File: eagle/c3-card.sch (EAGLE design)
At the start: 111 parts, among them J1 J-SAMTEC-TFM-110-X1-XXX-D-RA, J2 U.FL, J3 U.FL, J4 U.FL, J6 J-SAMTEC-TFM-120-X1-XXX-D-RA, J7 FTSH-105-XX-X-DV-K, Q3 MOSFET-PCH-SOT23-6, Q4 MOSFET-PCH-SOT23-6, Q5 PMV45EN, Q6 PMV45EN, U1 TCAN330, U2 IS21ES04G-JCLI-TR, U3 MAX7310ATE, U4 MAX4211CETE, U5 TPS62111RSA, U6 TCAN330, U7 MCP1703A, X1 16MHZ-2.5x2mm

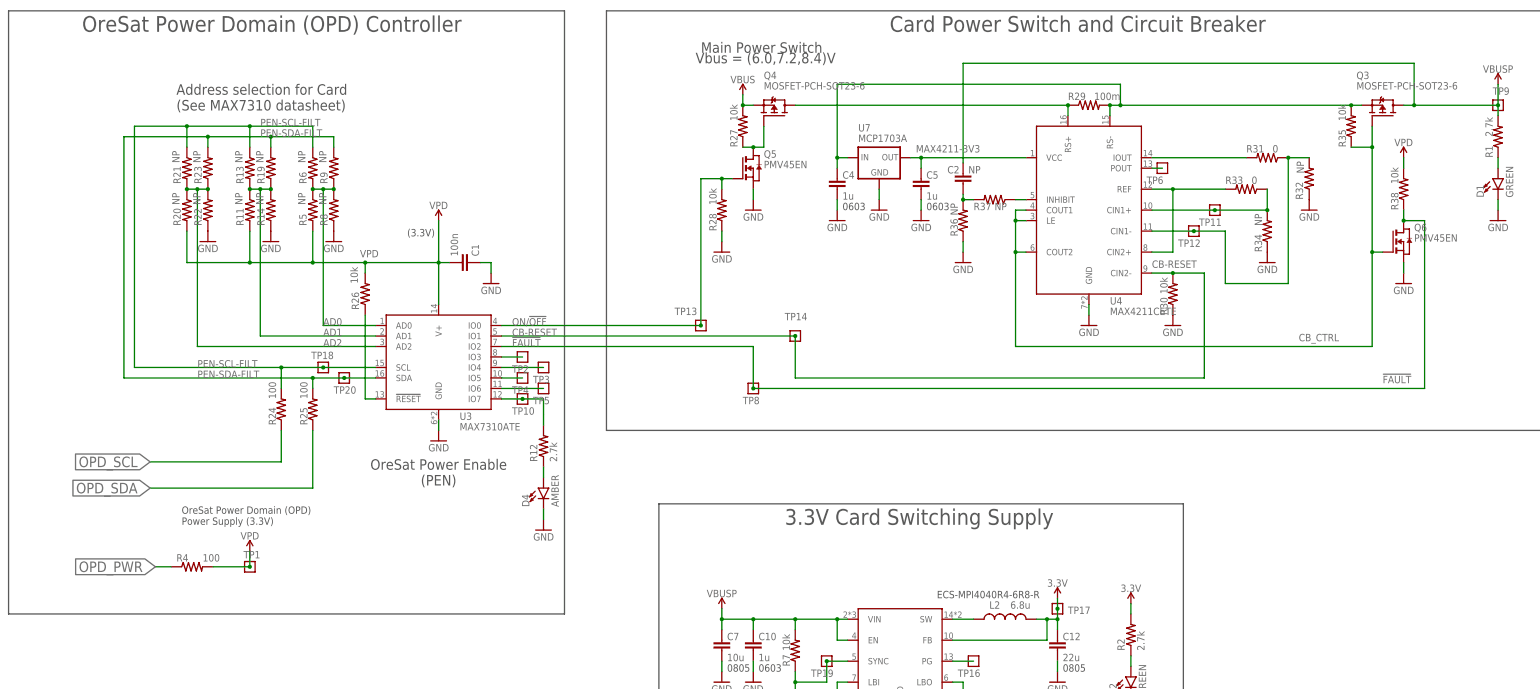
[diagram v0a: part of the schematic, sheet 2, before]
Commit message: Updated to the latest card outline. Updated OreSat main connector pinout. Got rid of some junk we don't need for C3.
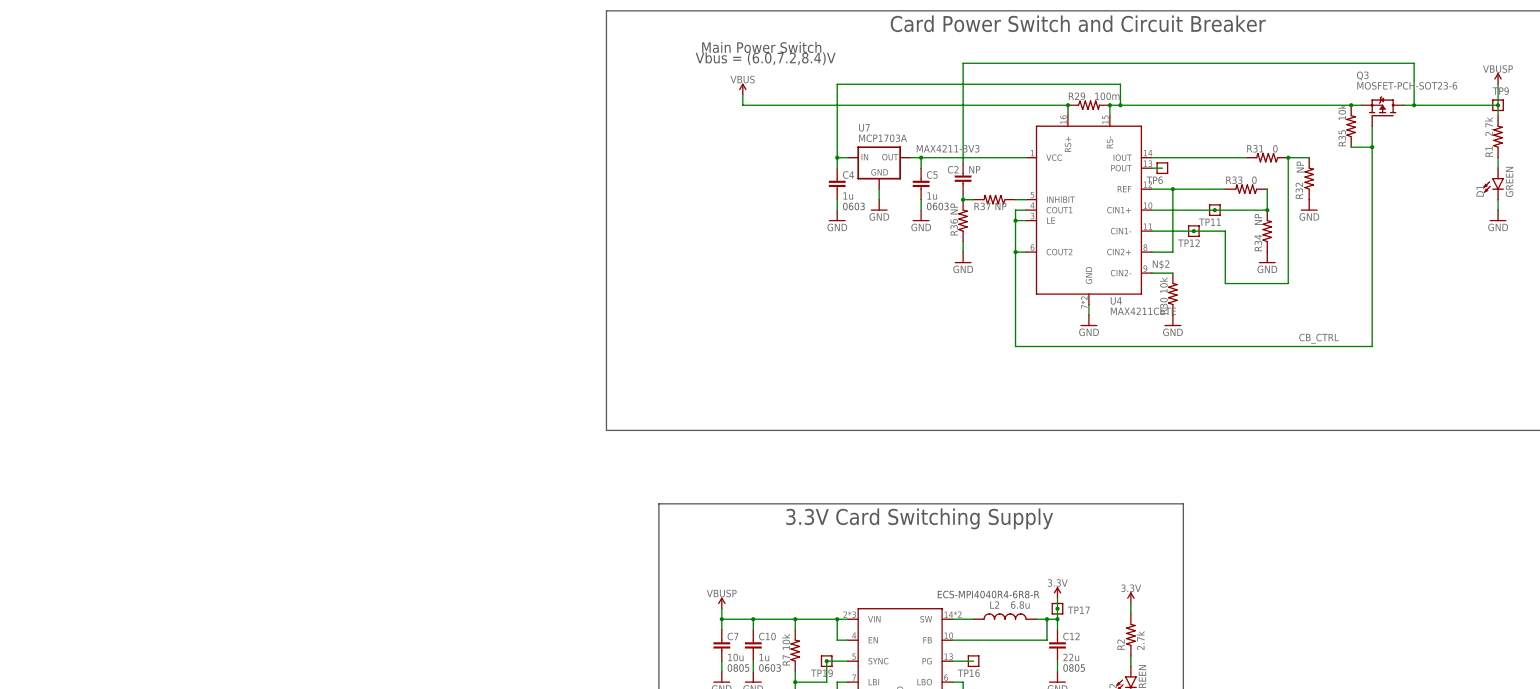
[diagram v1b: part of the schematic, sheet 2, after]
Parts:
- removed C1: 100n, rcl_custom:C-EU0402-B-NOSILK
- removed D4: AMBER, SparkFun-LED:LED-GREEN0603
- removed J1: J-SAMTEC-TFM-110-X1-XXX-D-RA, J-Samtec-TFM-110-X1-XXX-D-RA:J-SAMTEC-TFM-110-X1-XXX-D-RA
- removed J5: (no value), SparkFun-Connectors:6_PIN_SERIAL_TARGETSILK
- removed JP8: (no value), pinhead:PINHD-1X2
- removed Q4: MOSFET-PCH-SOT23-6, Q-MOSFET-PCH-SOT23-6:MOSFET-PCH-SOT23-6
- removed Q5, Q6: PMV45EN, Tova:PMV45EN
- removed R11, R13, R14, R19, R20, R21, R22, R23, R5, R6, R8, R9: NP, rcl_custom:R-US_0402-B-NOSILK
- removed R12: 2.7k, rcl_custom:R-US_0402-B-NOSILK
- removed R24, R25, R4: 100, rcl_custom:R-US_0402-B-NOSILK
- removed R26, R27, R28, R38: 10k, rcl_custom:R-US_0402-B-NOSILK
- removed TP1, TP10, TP13, TP14, TP18, TP2, TP20, TP3, TP4, TP5, TP8: TEST-POINT, Tova:TEST-POINT
- removed U3: MAX7310ATE, U-Maxim-MAX7310-I2C-GPIO-expander:MAX7310
- U$2: value ORESAT-CARD-V1.1 -> ORESAT-CARD-V1.1-3XRF; device oresat-cards:ORESAT-CARD-V1.1 -> oresat-cards:ORESAT-CARD-V1.1-3XRF
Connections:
- net !SHUTDOWN renamed !SD
- removed net !FAULT: Q6.D, R38.1, TP8.1, U3.IO2
- removed net AD0: R5.1, R6.2, R8.2, R9.1, U3.AD0
- removed net AD1: R11.1, R13.2, R14.2, R19.1, U3.AD1
- removed net AD2: R20.1, R21.2, R22.2, R23.1, U3.AD2
- removed net AUX_!SHUTDOWN: J1.19, J1.20
- removed net AUX_CAN1_H: J1.13, J1.14
- removed net AUX_CAN1_L: J1.15, J1.16
- removed net AUX_CAN2_H: J1.1, J1.2
- removed net AUX_CAN2_L: J1.3, J1.4
- removed net AUX_GND1: J1.17, J1.18
- removed net AUX_GND2: J1.11, J1.12
- removed net AUX_GND3: J1.10, J1.9
- removed net AUX_VBUS1: J1.7, J1.8
- removed net AUX_VBUS2: J1.5, J1.6
- removed net CB-RESET: R30.2, TP14.1, U3.IO1, U4.CIN2-
- removed net N$406: J5.VCC, JP8.2
- removed net N$480: TP2.1, U3.IO3
- removed net N$482: TP3.1, U3.IO4
- removed net N$518: TP4.1, U3.IO5
- removed net N$523: TP5.1, U3.IO6
- removed net N$573: R12.2, TP10.1, U3.IO7
- removed net N$575: D4.A, R12.1
- removed net N$589: R26.1, U3.!RESET
- removed net N$590: Q4.G, Q5.D, R27.1
- removed net N$593: Q4.D, R29.1, U4.RS+
- removed net ON/!OFF: Q5.G, R28.2, TP13.1, U3.IO0
- removed net PEN-SCL-FILT: R13.1, R21.1, R24.2, R6.1, TP18.1, U3.SCL
- removed net PEN-SDA-FILT: R19.2, R23.2, R25.2, R9.2, TP20.1, U3.SDA
- removed net SPARE6: J6.3, J6.4
- removed net SPARE7: J6.1, J6.2
- removed net VPD: C1.2, R11.2, R20.2, R26.2, R38.2, R4.2, R5.2, TP1.1, U3.V+
- new net N$2: R30.2, U4.CIN2-
- net CAN2_H: now also J6.17, J6.18; no longer J6.21, J6.22
- net CAN2_L: now also J6.19, J6.20; no longer J6.23, J6.24
- net CB_CTRL: no longer Q6.G
- net GND: now also J6.27, J6.28; no longer C1.1, D4.C, J5.GND, Q5.S, Q6.S, R14.1, R22.1, R28.1, R8.1, U3.GND
- net OPD_PWR: now also J6.15, J6.16; no longer J6.19, J6.20, R4.1
- net OPD_SCL: now also J6.13, J6.14; no longer J6.17, J6.18, R24.1
- net OPD_SDA: now also J6.11, J6.12; no longer J6.15, J6.16, R25.1
- net PA2/USART2_TX: no longer J5.TXO
- net PA3/USART2_RX: no longer J5.RXI
- net SPARE1: now also J6.10, J6.9; no longer J6.13, J6.14
- net SPARE2: now also J6.7, J6.8; no longer J6.11, J6.12
- net SPARE3: now also J6.5, J6.6; no longer J6.10, J6.9
- net SPARE4: now also J6.3, J6.4; no longer J6.7, J6.8
- net SPARE5: now also J6.1, J6.2; no longer J6.5, J6.6
- net VBUS: now also J6.21, J6.22, J6.23, J6.24, R29.1, U4.RS+; no longer J6.27, J6.28, Q4.S, R27.2
- net VBUSP: no longer JP8.1
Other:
- note removed: "(3.3V)"
- note removed: "Address selection for Card (See MAX7310 datasheet)"
- note removed: "Auxiliary Connector"
- note removed: "FTDI TTL-232R-3V3 cable"
- note removed: "OreSat Power Domain (OPD) Controller"
- note removed: "OreSat Power Domain (OPD) Power Supply (3.3V)"
- note removed: "OreSat Power Enable (PEN)"
- note removed: "Power VBUS from USB 5V (DEV ONLY)"

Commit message: Moved uC to new page
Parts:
- removed C11, C13, C18, C20, C21, C22, C23, C24, C25, C26, C3, C6, C8, C9: 100n, rcl_custom:C-EU0402-B-NOSILK
- removed C16, C17: 20p, rcl_custom:C-EU0402-B-NOSILK
- removed E2: (no value), oresat-rcl:L-BEAD-0603-B
- removed R17: 10k, rcl_custom:R-US_0402-B-NOSILK
- removed U$3: STM32F446ZET6, U-ST-STM32F446RE-uC:STM32F446ZET6
- removed U1, U6: TCAN330, TCAN330:TCAN330
- removed U2: IS21ES04G-JCLI-TR, IS21ES04G-JCLI-TR:IS21ES04G-JCLI-TR
- removed X1: 16MHZ-2.5x2mm, low-gain-radio:CRYSTAL-WITH-GND
- added C1, C14, C15, C19, C27, C28, C29, C32, C33, C34, C35, C36, C37, C38: 100n, rcl_custom:C-EU0402-B-NOSILK
- added C30, C31: 20p, rcl_custom:C-EU0402-B-NOSILK
- added E1: (no value), oresat-rcl:L-BEAD-0603-B
- added R4: 10k, rcl_custom:R-US_0402-B-NOSILK
- added U$1: STM32F446ZET6, U-ST-STM32F446RE-uC:STM32F446ZET6
- added U3, U8: TCAN330, TCAN330:TCAN330
- added U9: IS21ES04G-JCLI-TR, IS21ES04G-JCLI-TR:IS21ES04G-JCLI-TR
- added X2: 16MHZ-2.5x2mm, low-gain-radio:CRYSTAL-WITH-GND
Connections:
- removed net CRYSTALIN2: C17.1, U$3.PH1, X1.1
- removed net CRYSTALOUT2: C16.1, U$3.PH0, X1.2
- removed net N$6: R17.2, U$3.BOOT0
- removed net N$7: E2.2, U$3.VDDA
- new net CRYSTALIN1: C31.1, U$1.PH1, X2.1
- new net CRYSTALOUT1: C30.1, U$1.PH0, X2.2
- new net N$3: R4.2, U$1.BOOT0
- new net N$4: E1.2, U$1.VDDA
- net 3.3V: now also C1.2, C14.2, C15.2, C19.2, C27.2, C28.2, C29.2, C32.2, C33.2, C34.2, C35.2, C36.2, C37.2, C38.2, E1.1, U$1.VBAT, U$1.VDD, U3.VCC, U8.VCC, U9.VCC, U9.VCCQ; no longer C11.2, C13.2, C18.2, C20.2, C21.2, C22.2, C23.2, C24.2, C25.2, C26.2, C3.2, C6.2, C8.2, C9.2, E2.1, U$3.VBAT, U$3.VDD, U1.VCC, U2.VCC, U2.VCCQ, U6.VCC
- net CAN1_H: now also U3.CANH; no longer U1.CANH
- net CAN1_L: now also U3.CANL; no longer U1.CANL
- net CAN1_RX: now also U$1.PA11, U3.RXD; no longer U$3.PA11, U1.RXD
- net CAN1_SHDN: now also U$1.PA10, U3.SHDN; no longer U$3.PA10, U1.SHDN
- net CAN1_SILENT: now also U$1.PA9, U3.S; no longer U$3.PA9, U1.S
- net CAN1_TX: now also U$1.PA12, U3.TXD; no longer U$3.PA12, U1.TXD
- net CAN2_H: now also U8.CANH; no longer U6.CANH
- net CAN2_L: now also U8.CANL; no longer U6.CANL
- net CAN2_RX: now also U$1.PB12, U8.RXD; no longer U$3.PB12, U6.RXD
- net CAN2_SHDN: now also U$1.PB11, U8.SHDN; no longer U$3.PB11, U6.SHDN
- net CAN2_SILENT: now also U$1.PB10, U8.S; no longer U$3.PB10, U6.S
- net CAN2_TX: now also U$1.PB13, U8.TXD; no longer U$3.PB13, U6.TXD
- net GND: now also C1.1, C14.1, C15.1, C19.1, C27.1, C28.1, C29.1, C30.2, C31.2, C32.1, C33.1, C34.1, C35.1, C36.1, C37.1, C38.1, R4.1, U$1.VSS, U$1.VSSA, U3.GND, U8.GND, U9.VSS, U9.VSSQ, X2.SHIELD; no longer C11.1, C13.1, C16.2, C17.2, C18.1, C20.1, C21.1, C22.1, C23.1, C24.1, C25.1, C26.1, C3.1, C6.1, C8.1, C9.1, R17.1, U$3.VSS, U$3.VSSA, U1.GND, U2.VSS, U2.VSSQ, U6.GND, X1.SHIELD
- net NRESET: now also U$1.NRST; no longer U$3.NRST
- net PA0: now also U$1.PA0; no longer U$3.PA0
- net PA2/USART2_TX: now also U$1.PA2; no longer U$3.PA2
- net PA3/USART2_RX: now also U$1.PA3; no longer U$3.PA3
- net SWCLK: now also U$1.PA14; no longer U$3.PA14
- net SWDIO: now also U$1.PA13; no longer U$3.PA13
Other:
- moved on the sheet: D3, J7, R3
